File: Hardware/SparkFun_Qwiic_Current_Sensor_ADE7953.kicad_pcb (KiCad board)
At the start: 2 copper layers, 25.4 x 25.4 mm, 85 parts, among them J1 Qwiic_RA, J2 Qwiic_RA, J3 Conn_01x06, J4 Conn_01x02, J5 3.5mm TRRS, J6 Conn_01x02, U1 ADE7953ACPZ, Y1 3.579545MHz

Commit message: Changed 4x4 chip size to 5x5mm
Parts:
- U1: footprint SparkFun-Semiconductor-Standard:QFN-28-1EP_4x4_5mmx5mm -> SparkFun-Semiconductor-Standard:QFN-28-1EP_4x4_5x5mm
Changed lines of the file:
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@@
 		)
 	)
-	(footprint "SparkFun-Semiconductor-Standard:QFN-28-1EP_4x4_5mmx5mm"
+	(footprint "SparkFun-Semiconductor-Standard:QFN-28-1EP_4x4_5x5mm"
 		(layer "F.Cu")
 		(at 135.966 101.5985 180)
-		(descr "ADE7953ACPZ")
+		(descr "QFN-28-1EP_4x4_5x5mm")
 		(tags "Integrated Circuit")
 		(property "Reference" "U1"
-			(at 0 0 180)
-			(layer "F.SilkS")
+			(at -2.1 -4.2 180)
+			(layer "F.Fab")
 			(effects
 				(font
@@
 		(property "Value" "ADE7953ACPZ"
 			(at 0 0 180)
-			(layer "F.SilkS")
+			(layer "F.Fab")
 			(hide yes)
 			(effects
@@
 			)
 		)
-		(property "Datasheet" ""
+		(property "Datasheet" "https://www.mouser.in/datasheet/2/609/ADE7953-3120226.pdf"
 			(at 0 0 180)
 			(layer "F.Fab")
@@
 			)
 		)
-		(property "Description" ""
+		(property "Description" "Single Phase Multifunction Metering IC with Neutral Current Measurement"
 			(at 0 0 180)
 			(layer "F.Fab")
@@
 		(attr smd)
 		(fp_circle
-			(center -2.9 -2.25)
-			(end -2.9 -2.125)
-			(stroke
-				(width 0.25)
-				(type solid)
-			)
-			(fill no)
+			(center -2.7 -2.7)
+			(end -2.7 -2.6)
+			(stroke
+				(width 0.2)
+				(type solid)
+			)
+			(fill yes)
 			(layer "F.SilkS")
 		)
@@
 		)
 		(fp_text user "${REFERENCE}"
-			(at 0 0 180)
+			(at 0 4.4 180)
 			(layer "F.Fab")
 			(effects
@@
 				)
 			)
+		)
+		(pad "" smd roundrect
+			(at -0.7 -0.7 180)
+			(size 1.2625 1.325)
+			(layers "F.Paste")
+			(roundrect_rratio 0.238095)
+		)
+		(pad "" smd roundrect
+			(at -0.7 0.7 180)
+			(size 1.2625 1.325)
+			(layers "F.Paste")
+			(roundrect_rratio 0.238095)
+		)
+		(pad "" smd roundrect
+			(at 0.7 -0.7 180)
+			(size 1.2625 1.325)
+			(layers "F.Paste")
+			(roundrect_rratio 0.238095)
+		)
+		(pad "" smd roundrect
+			(at 0.7 0.7 180)
+			(size 1.2625 1.325)
+			(layers "F.Paste")
+			(roundrect_rratio 0.238095)
 		)
 		(pad "1" smd rect
@@
 			(at 0 0 180)
 			(size 3.24 3.24)
-			(layers "F.Cu" "F.Mask" "F.Paste")
+			(layers "F.Cu" "F.Mask")
 			(net 1 "GND")
 			(pinfunction "EP")

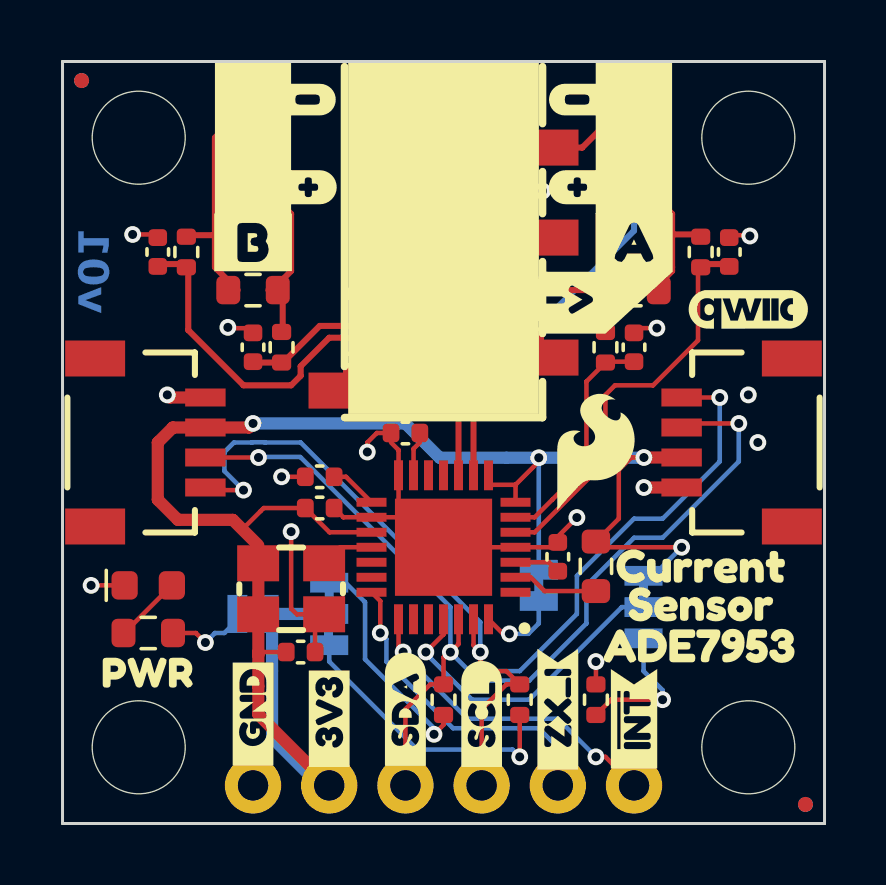
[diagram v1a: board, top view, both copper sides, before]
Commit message: Updated number for Reds, added I2C Addr
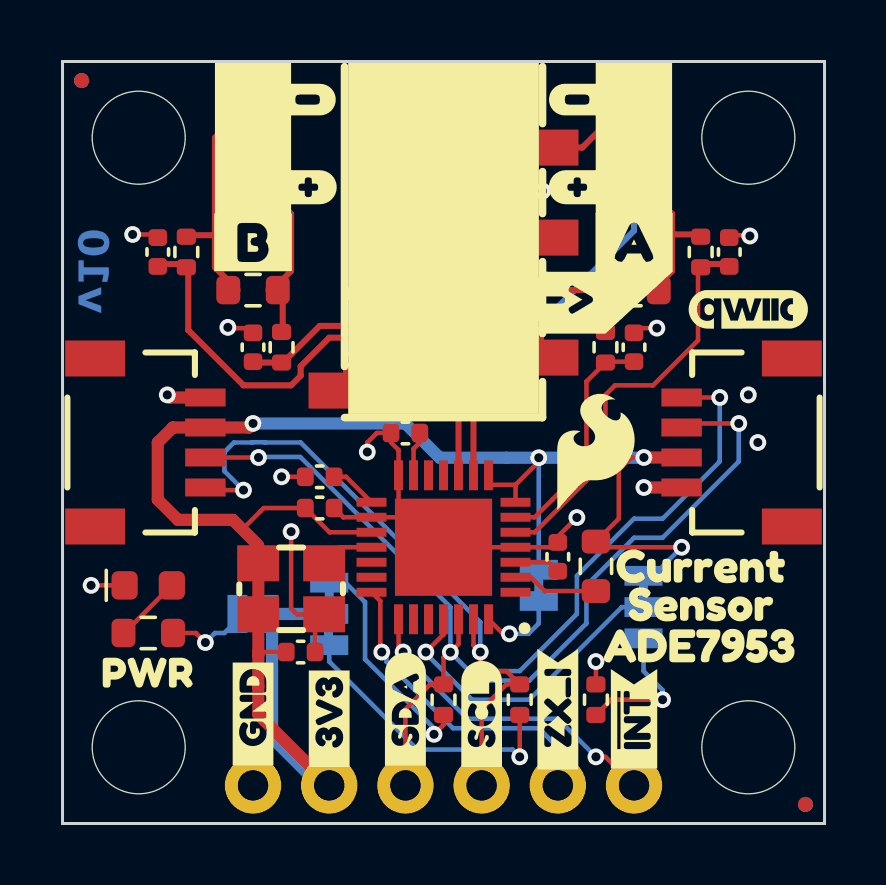
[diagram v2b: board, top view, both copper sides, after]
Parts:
- added kibuzzard-6A3051E6: G***, kibuzzard-6A3051E6, B.Cu at (127.7, 101.9)
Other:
- board text added: "v10"
- board text removed: "v01"

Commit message: Updated PCB based on Design Review II feedback
- Updated schematic I2C labels
- Updated component silkscreens and courtyards
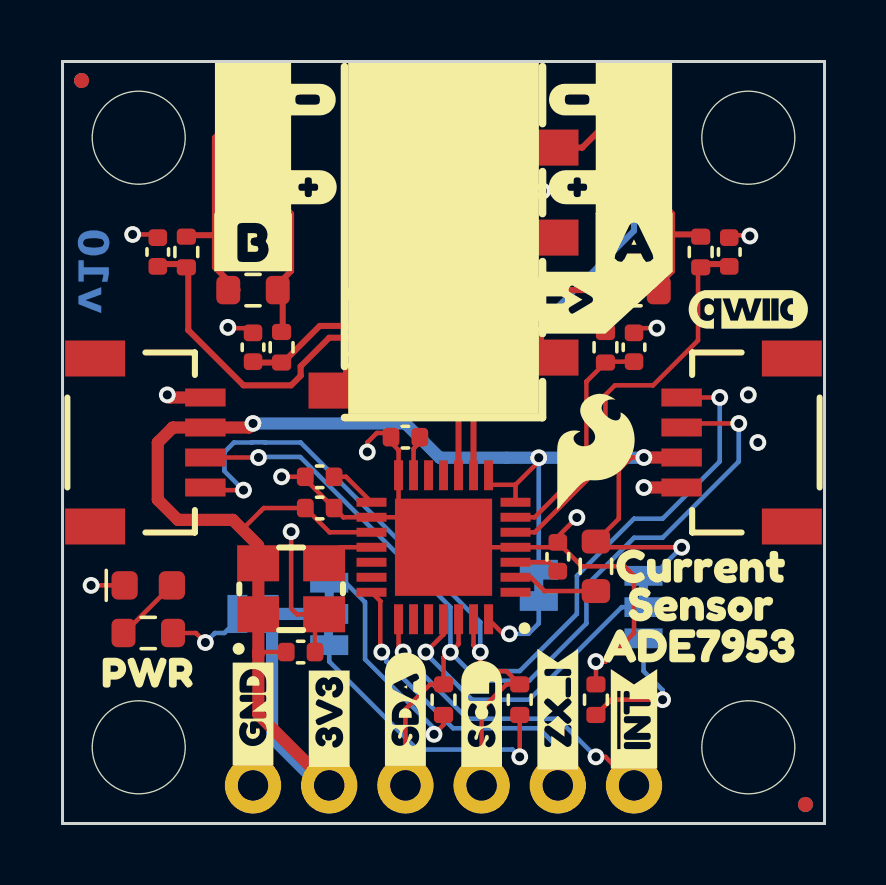
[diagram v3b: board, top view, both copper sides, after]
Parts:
- moved C1 0.14 mm to (134.7, 97.9)
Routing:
- net 3.3V: track 63.2 -> 61.7 mm
- net GND: track 31.4 -> 32.4 mm
- net B+: track 6.01 -> 5.47 mm
